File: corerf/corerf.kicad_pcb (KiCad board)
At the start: 2 copper layers, 55.9 x 35.6 mm, 16 parts, among them J1 I2C_1, J2 I2C_2, J3 CoreRF-Header, J4 ISP, J5 JTAG, J6 USB_B_Mini, U1 LDO-3V3, U2 HT42B534-1SOP10

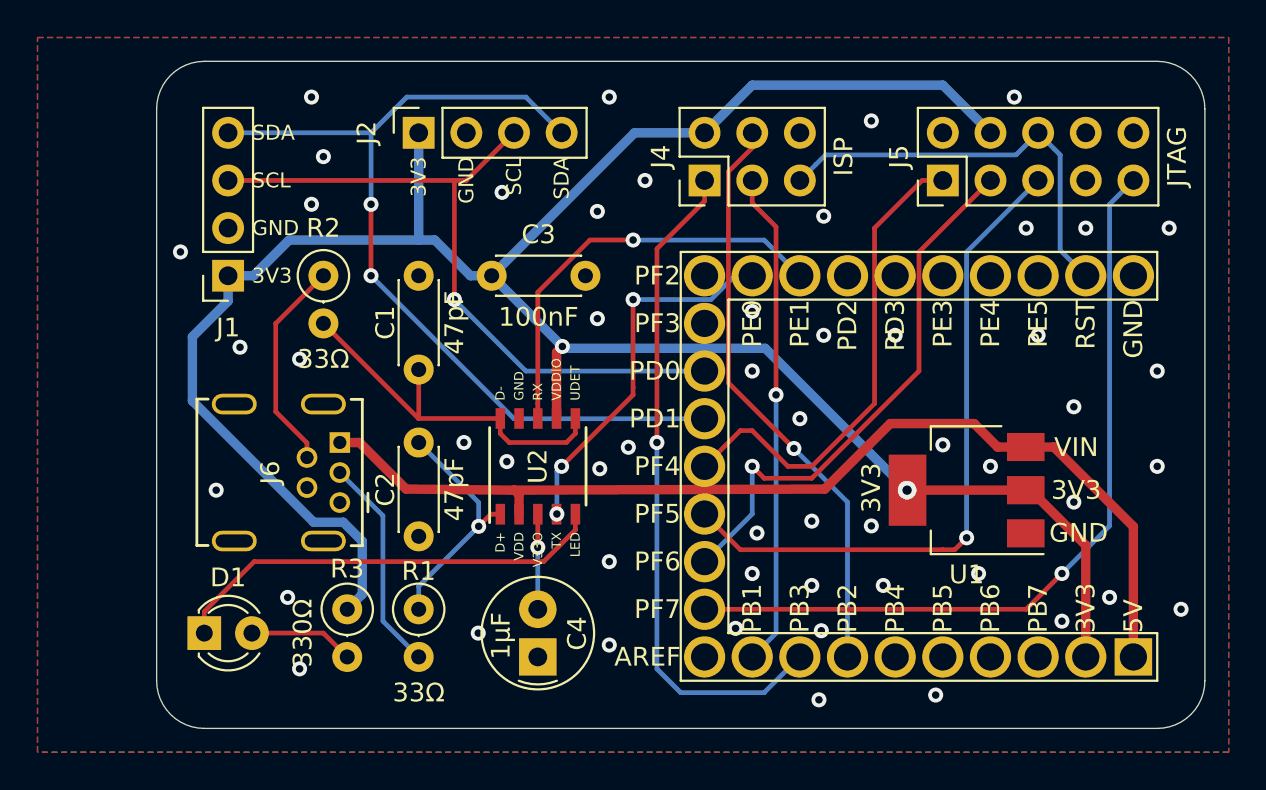
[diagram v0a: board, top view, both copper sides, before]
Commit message: treewide: Update to KiCAD 7
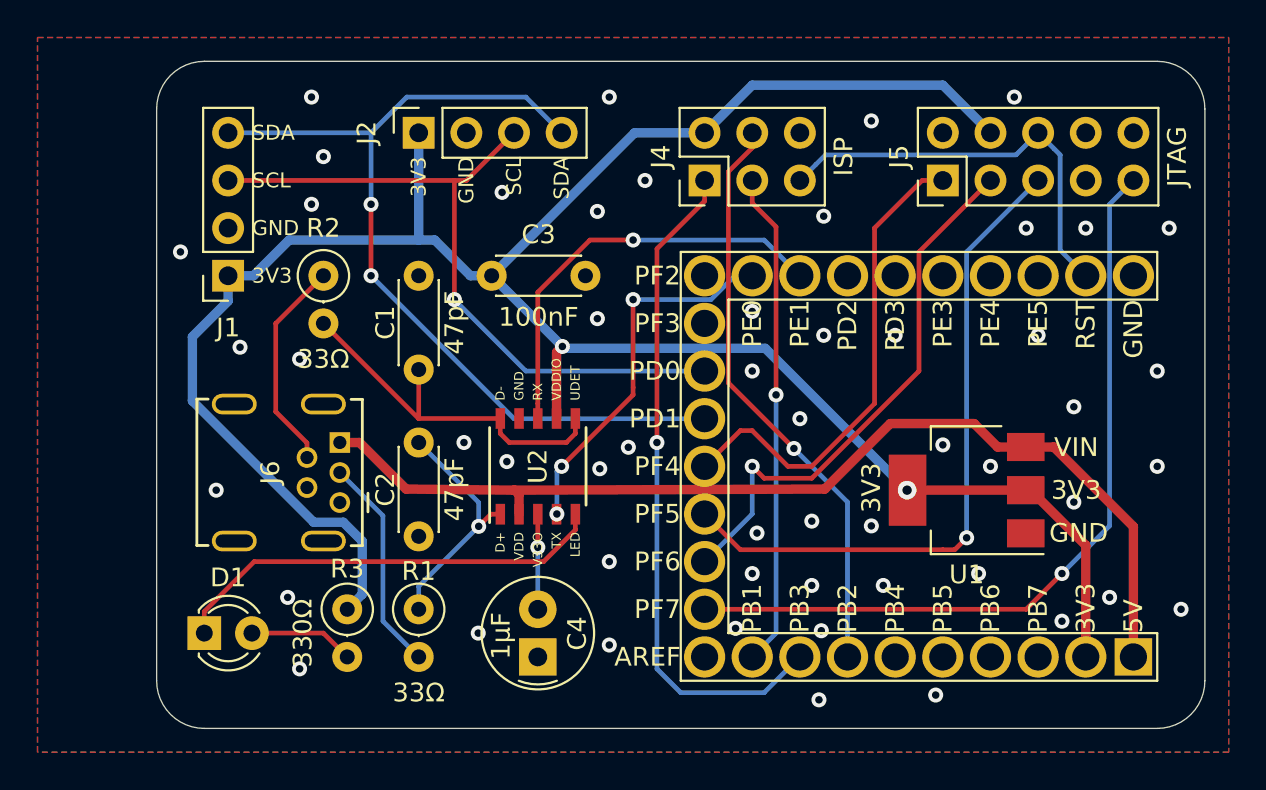
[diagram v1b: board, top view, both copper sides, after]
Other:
- net class Default removed
- net class Power removed
